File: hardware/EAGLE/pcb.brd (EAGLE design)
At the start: 17.8 x 110.5 mm, 46 parts, among them IC1 4017N, IC2 DG412DJD, IC3 DG412DJD, J1 2x5 pin header, Q1 MMBT3904, Q2 MMBT3904, Q3 MMBT3904, Q4 MMBT3904

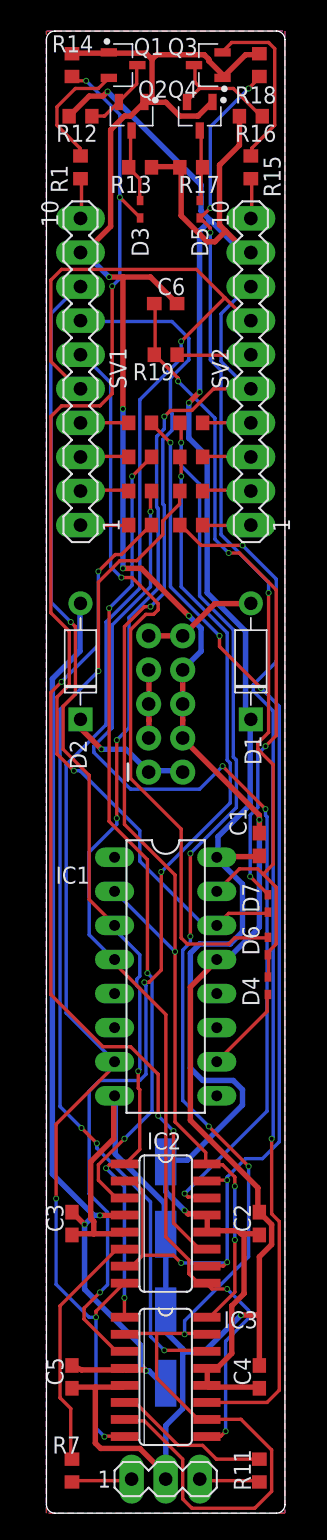
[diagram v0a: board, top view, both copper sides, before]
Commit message: Transistor footprint fixed
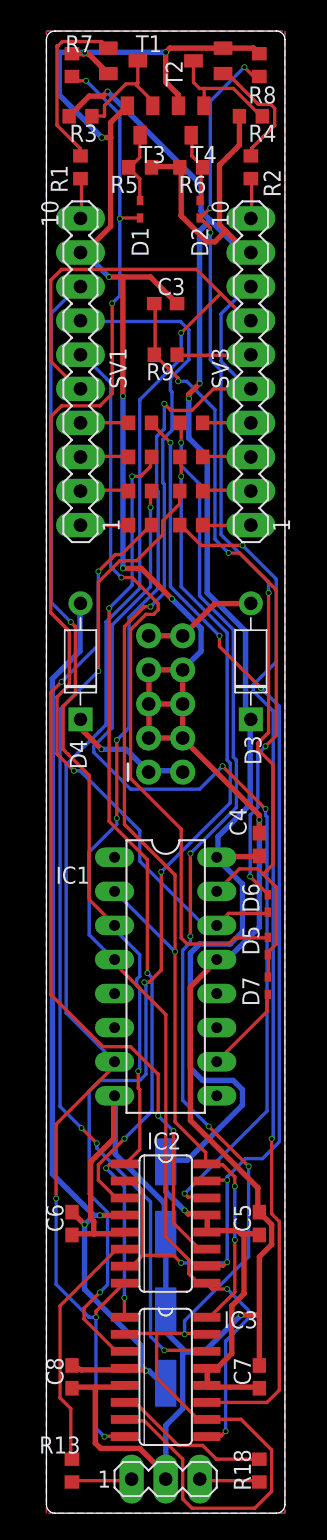
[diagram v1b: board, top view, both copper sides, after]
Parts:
- removed Q1, Q2, Q3, Q4: MMBT3904, Transistor:SOT95P237X112-3N
- added T1, T2, T3, T4: MMBT3904, transistor:SOT23-BEC
- C1, C2: value 100n -> 10u; device rcl:C0603 -> rcl:153CLV-0605
- C7, C8: value 10u -> 100n; device rcl:153CLV-0605 -> rcl:C0603
- D1, D2: value 1N4004 -> 1N4148WT; device Diodes:DO-41 -> diode:SOD523
- D3, D4: value 1N4148WT -> 1N4004; device diode:SOD523 -> Diodes:DO-41
- R12, R13, R16, R17, R19: value 10k -> 1k
- R14, R15, R18: value 47k -> 1k
- R2, R7, R8: value 1k -> 47k
- R3, R4, R5, R6, R9: value 1k -> 10k
- SV2: value 1x10 pin header -> 1x3 pin header; device con-lstb:MA10-1 -> con-lstb:MA03-1
- SV3: value 1x3 pin header -> 1x10 pin header; device con-lstb:MA03-1 -> con-lstb:MA10-1
- moved R18 104.8 mm to (17.1, 12.1), turned to 270 degrees
- moved R7 104.8 mm to (3.17, 116.8), turned to 90 degrees
- moved R13 97.3 mm to (3.17, 12.1), turned to 270 degrees
- moved SV2 82.8 mm to (10.2, 11.4), turned to 0 degrees
- moved SV3 82.8 mm to (16.5, 94.0), turned to 90 degrees
- moved R11 73.6 mm to (8.26, 85.1), turned to 180 degrees
- moved C3 68.9 mm to (10.2, 99.1), turned to 0 degrees
- moved C6 68.9 mm to (3.17, 30.5), turned to 90 degrees
- moved D5 55.2 mm to (17.8, 51.1)
- moved C4 39.7 mm to (17.1, 58.7)
- moved D2 34.8 mm to (12.7, 106.0)
- moved D1 34.7 mm to (8.26, 106.0)
- moved D3 34.7 mm to (16.5, 72.4)
- moved R12 30.8 mm to (8.26, 82.5)
- moved R8 29.6 mm to (17.1, 116.8), turned to 90 degrees
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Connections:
- net +12V: now also C1.+, C5.1, C7.1, D3.C, R3.2, R4.2, R5.2, R6.2, SV3.9; no longer C1.1, C2.1, C7.+, D1.C, R12.2, R13.2, R16.2, R17.2, SV2.9
- net -12V: now also C2.-, C6.2, C8.2, D4.A; no longer C3.2, C5.2, C8.-, D2.A
- net BUTTON: now also R9.1, SV3.6; no longer R19.1, SV2.6
- net CLK: now also D1.C, D6.C, R7.1; no longer D3.C, D7.C, R14.1
- net GND: now also C1.-, C2.+, C3.2, C5.2, C6.1, C7.2, C8.1, R7.2, R8.2, SV2.2, T1.E, T2.E, T3.E, T4.E; no longer C1.2, C2.2, C3.1, C5.1, C6.2, C7.-, C8.+, Q1.1, Q2.1, Q3.1, Q4.1, R14.2, R18.2, SV3.2
- net IO1A: now also R10.2; no longer R4.2
- net IO1B: now also R15.2, SV3.3; no longer R8.2, SV2.3
- net IO2A: now also R11.2; no longer R5.2
- net IO2B: now also R16.2, SV3.2; no longer R9.2, SV2.2
- net IO3A: now also R12.2; no longer R6.2
- net IO3B: now also R17.2, SV3.1; no longer R10.2, SV2.1
- net IO4A: now also R13.2, SV2.1; no longer R7.2, SV3.1
- net IO4B: now also R18.2, SV2.3; no longer R11.2, SV3.3
- net N$1: now also D3.A; no longer D1.A
- net N$10: now also R16.1; no longer R9.1
- net N$11: now also R17.1; no longer R10.1
- net N$12: now also R18.1; no longer R11.1
- net N$13: now also C3.1, D6.A, R9.2; no longer C6.1, D7.A, R19.2
- net N$14: now also T1.B; no longer Q1.2
- net N$15: now also R3.1, T1.C, T3.B; no longer Q1.3, Q2.2, R12.1
- net N$16: now also D1.A, R5.1, T3.C; no longer D3.A, Q2.3, R13.1
- net N$17: now also D7.A; no longer D4.A
- net N$19: now also R2.2, T2.B; no longer Q3.2, R15.2
- net N$2: now also D4.C; no longer D2.C
- net N$20: now also R4.1, T2.C, T4.B; no longer Q3.3, Q4.2, R16.1
- net N$21: now also D2.A, R6.1, T4.C; no longer D5.A, Q4.3, R17.1
- net N$3: now also R14.1; no longer R2.1
- net N$4: now also R10.1; no longer R4.1
- net N$5: now also R19.1; no longer R3.1
- net N$6: now also R11.1; no longer R5.1
- net N$7: now also R12.1; no longer R6.1
- net N$8: now also R13.1; no longer R7.1
- net N$9: now also R15.1; no longer R8.1
- net NO: now also D5.A; no longer D6.A
- net OIA: now also R14.2; no longer R2.2
- net OIB: now also R19.2, SV3.4; no longer R3.2, SV2.4
- net Q2: now also SV3.5, SV3.8; no longer SV2.5, SV2.8
- net Q3: now also SV3.7; no longer SV2.7
- net RES: now also D2.C, D7.C, R8.1; no longer D4.C, D6.C, R18.1
- net RESET: now also R2.1, SV3.10; no longer R15.1, SV2.10
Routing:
- net GND: track 214.6 -> 227.3 mm, vias 6 -> 9
- net N$19: track 13.2 -> 9.25 mm
- net N$14: track 9.17 -> 13.1 mm
- net N$15: track 5.77 -> 8.70 mm
- net RES: track 77.3 -> 78.9 mm
- net Q2: track 103.3 -> 104.3 mm
- net CLK: track 82.2 -> 81.5 mm

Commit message: Fixed some layout issues
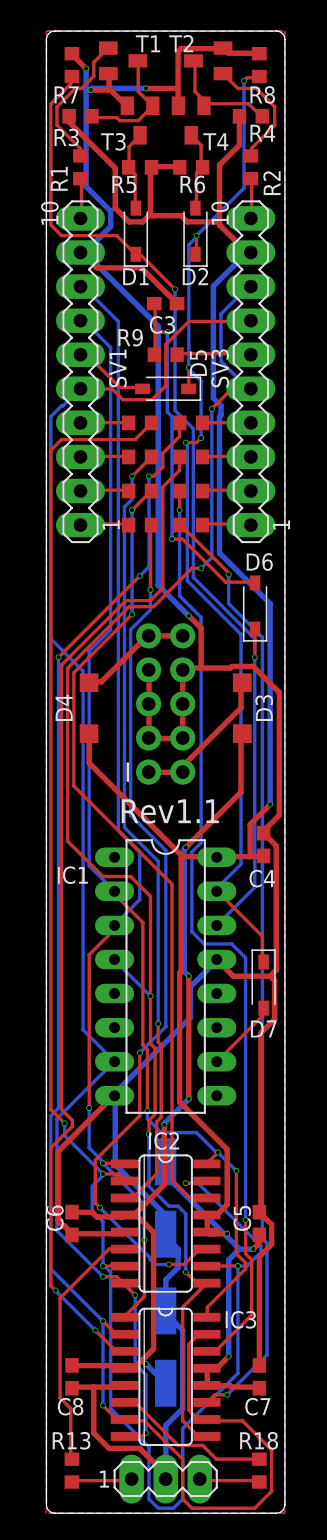
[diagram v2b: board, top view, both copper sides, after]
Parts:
- D1, D2, D5, D6, D7: value 1N4148WT -> 1N4148W; device diode:SOD523 -> Diode:SOD3715X135
- D3, D4: value 1N4004 -> (none); device Diodes:DO-41 -> diode:SOD123
- moved D5 42.3 mm to (10.2, 92.7), turned to 180 degrees
- moved D6 22.2 mm to (16.8, 76.5)
- moved D3 3.55 mm to (15.9, 68.9), turned to 270 degrees
- moved D4 3.55 mm to (4.45, 68.9)
- moved D1 1.62 mm to (7.94, 104.5)
- moved D2 1.62 mm to (12.4, 104.5)
- moved D7 0.32 mm to (17.5, 48.3)
- moved C4 0.32 mm to (17.5, 58.7)
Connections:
- removed net N$17: D7.A, IC1.10
- new net Q4: D7.2, IC1.10
- net +12V: now also D4.C; no longer D3.C
- net -12V: now also D3.A; no longer D4.A
- net CLK: now also D1.1, D6.1; no longer D1.C, D6.C
- net N$1: now also D4.A; no longer D3.A
- net N$13: now also D6.2; no longer D6.A
- net N$16: now also D1.2; no longer D1.A
- net N$2: now also D3.C; no longer D4.C
- net N$21: now also D2.2; no longer D2.A
- net NO: now also D5.2; no longer D5.A
- net RES: now also D2.1, D5.1, D7.1; no longer D2.C, D5.C, D7.C
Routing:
- net NO: track 56.1 -> 5.68 mm, vias 1 -> 0
- net N$3: track 86.8 -> 130.0 mm, vias 6 -> 5
- net N$13: track 50.1 -> 27.9 mm, vias 4 -> 2
- net Q3: track 126.1 -> 105.0 mm, vias 4 -> 3
- net Q1: track 95.9 -> 84.8 mm, vias 4 -> 3
- net N$6: track 70.3 -> 60.0 mm, vias 4 -> 2
- net GND: track 227.3 -> 236.9 mm, vias 9 -> 4
- net -12V: track 72.7 -> 65.1 mm, vias 3 -> 5
- net N$17: track 6.62 -> 0.00 mm
- net N$11: track 76.7 -> 70.5 mm
- net Q4: track 0.00 -> 5.48 mm
- net CLK: track 81.5 -> 76.1 mm, vias 4 -> 2
- net N$10: track 74.9 -> 69.9 mm, vias 4 -> 2
- net Q2: track 104.3 -> 108.4 mm
- net +12V: track 158.0 -> 160.5 mm
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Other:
- board text added: "Rev1.1"

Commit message: Added smd 4017 footprint
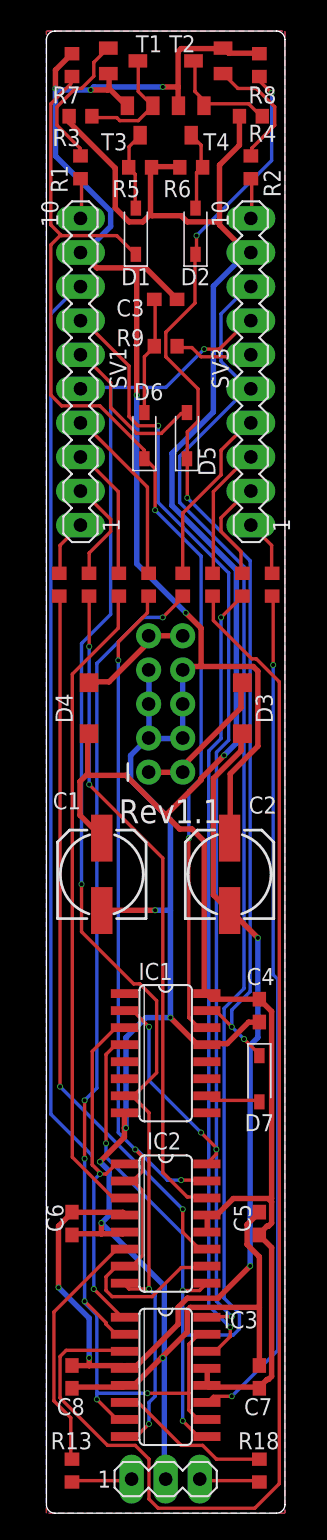
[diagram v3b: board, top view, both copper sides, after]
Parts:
- IC1: value 4017N -> 4017D; device 40xx:DIL16 -> 40xx:SO16
- moved C2 35.6 mm to (14.9, 56.5), flipped to the top
- moved C1 24.6 mm to (5.40, 56.5), flipped to the top
- moved D6 15.1 mm to (8.57, 89.2)
- moved C4 12.4 mm to (17.1, 46.4), turned to 270 degrees
- moved R14 12.1 mm to (8.89, 78.1), turned to 90 degrees
- moved R19 12.1 mm to (11.4, 78.1), turned to 90 degrees
- moved R10 9.66 mm to (6.67, 78.1), turned to 90 degrees
- moved R15 9.66 mm to (13.7, 78.1), turned to 90 degrees
- moved R11 7.96 mm to (4.45, 78.1), turned to 90 degrees
- moved R16 7.96 mm to (15.9, 78.1), turned to 90 degrees
- moved R12 7.49 mm to (2.22, 78.1), turned to 90 degrees
- moved R17 7.49 mm to (18.1, 78.1), turned to 90 degrees
- moved D7 6.99 mm to (17.1, 41.3)
- moved IC1 5.72 mm to (10.2, 43.2)
- moved D5 3.84 mm to (11.7, 89.2), turned to 90 degrees
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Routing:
- net N$3: track 130.0 -> 72.1 mm, vias 5 -> 3
- net N$5: track 116.2 -> 86.0 mm, vias 5 -> 6
- net N$9: track 75.1 -> 98.8 mm, vias 2 -> 0
- net N$13: track 27.9 -> 8.82 mm, vias 2 -> 0
- net Q2: track 108.4 -> 125.3 mm, vias 5 -> 3
- net Q1: track 84.8 -> 97.5 mm, vias 3 -> 5
- net N$7: track 65.2 -> 53.6 mm, vias 4 -> 2
- net -12V: track 65.1 -> 76.5 mm, vias 5 -> 4
- net Q0: track 84.3 -> 95.4 mm, vias 3 -> 2
- net N$10: track 69.9 -> 59.1 mm
- net N$6: track 60.0 -> 49.3 mm
- net GND: track 236.9 -> 226.6 mm, vias 4 -> 11
- net N$4: track 58.8 -> 48.4 mm, vias 2 -> 0
- net OIA: track 3.60 -> 13.5 mm
- net CLK: track 76.1 -> 86.0 mm
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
